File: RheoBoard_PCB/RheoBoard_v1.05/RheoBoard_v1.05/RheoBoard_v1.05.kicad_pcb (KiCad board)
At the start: 2 copper layers, 109 x 126.4 mm, 160 parts, among them J1 JST SH 4-pin 1.00mm, J12 JST SH 4-pin 1.00mm, J17 JST SH 4-pin 1.00mm, J19 BUTTONS_GPIO, J2 PJ-082BH, J3 JST EH 4-pin 2.50mm, J9 JST SH 4-pin 1.00mm, Q10 AO3400A, Q11 DMP6023LE-13, Q3 AO3400A, Q4 AO3400A, Q8 AO3400A, SW1 TL3301NF160QG/P010515, SW2 TL3301NF160QG/P010515, SW3 TL3301NF160QG/P010515, SW4 TL3301NF160QG/P010515, U1 TPS563203DRLR, U10 JST XH 2-pin 2.50mm, U11 ZR370-02PM / 4.5V / 2.5 LPM /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, U12 TPS259472ARPWR, U13 TCA9517ADGKR, U2 TPS563203DRLR, U3 TPS563203DRLR, U5 MPRLS0025PA00001A, U7 PCA9685PW,118, U8 ZR370-02PM / 4.5V / 2.5 LPM /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, U9 JST XH 2-pin 2.50mm

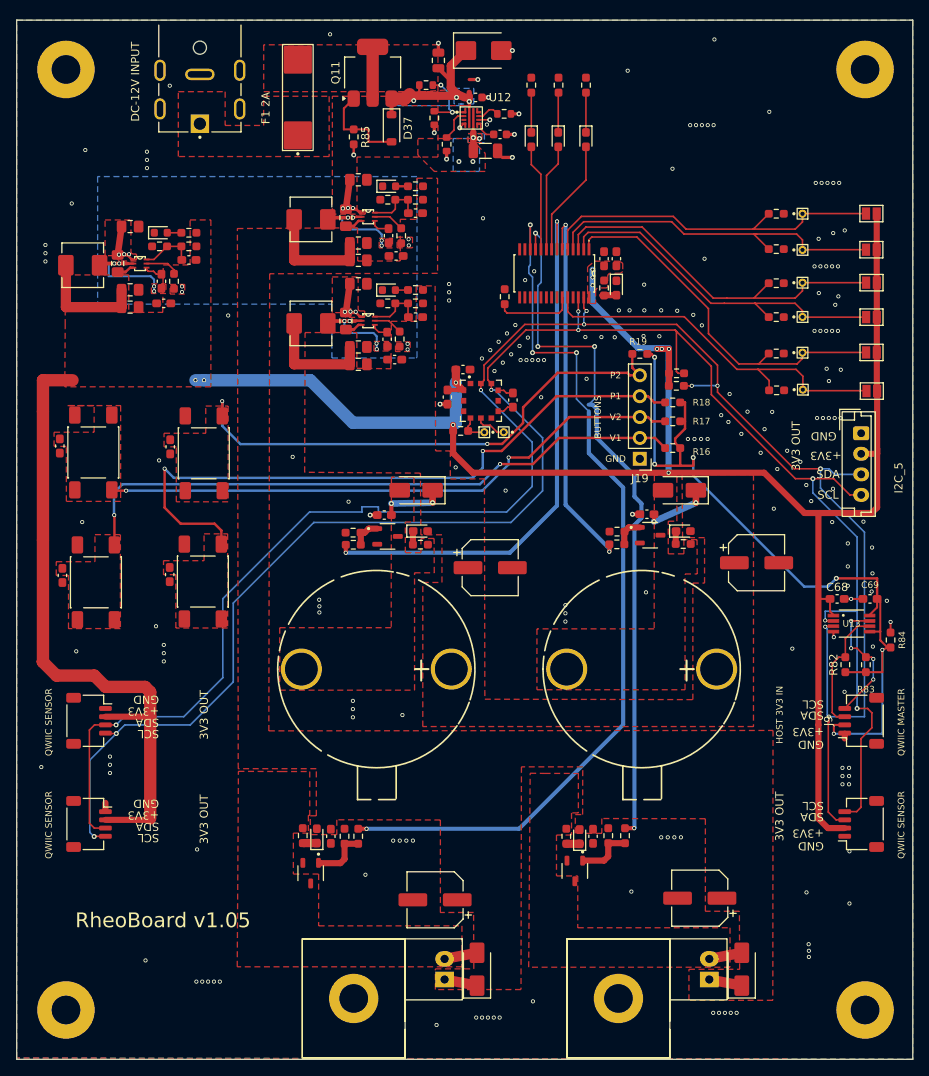
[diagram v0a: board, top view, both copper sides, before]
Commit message: Update RheoBoard v1.05 documentation and manufacturing files. Refined assembly and bringup notes to include updated LED polarity and connector specifications. Corrected footprint and layout details based on recent reviews, ensuring alignment with TI recommendations. Enhanced revision notes to reflect changes in component placements and routing adjustments, including improved via organization and updated BOM references. Manufacturing files, including Gerber and assembly drawings, have been refreshed for accuracy in production.
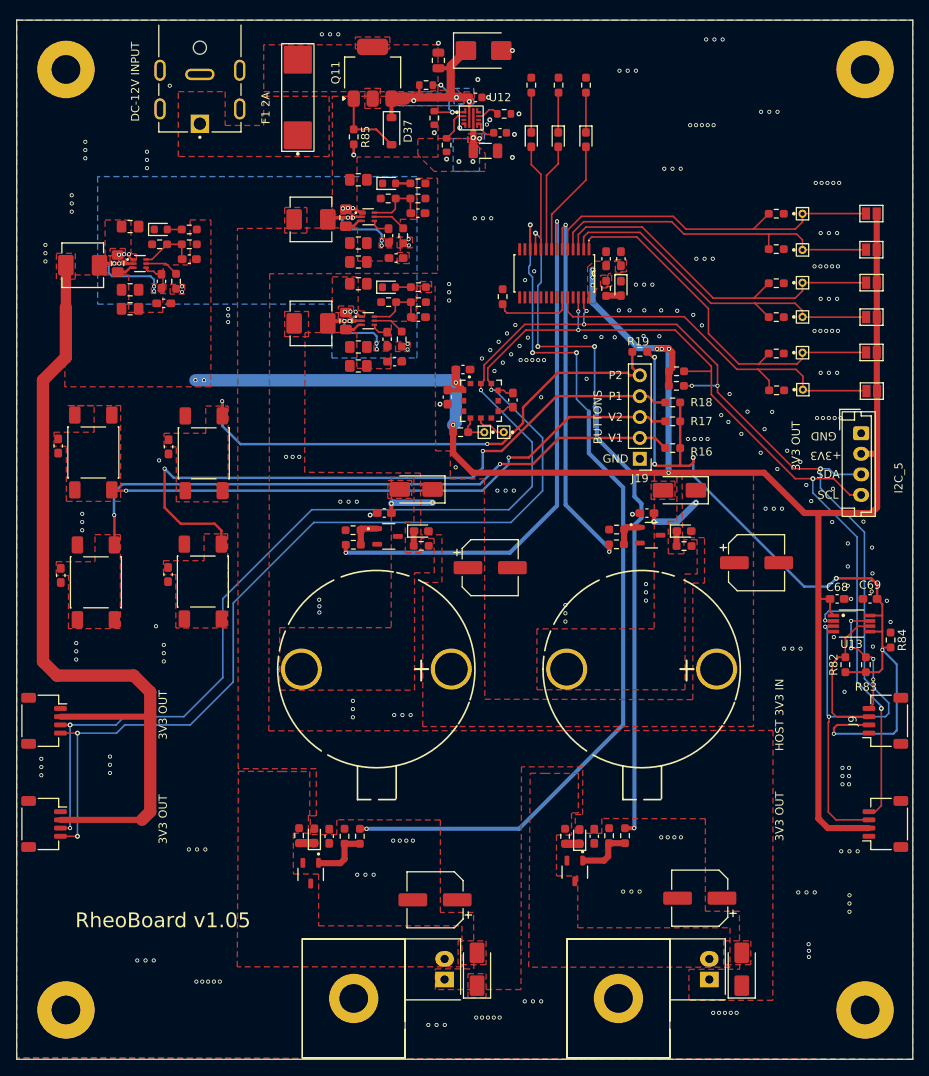
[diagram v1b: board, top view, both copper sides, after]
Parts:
- D13, D14, D15, D17, D19, D6, D7, D8: footprint LED_SMD:LED_0603_1608Metric_Pad1.05x0.95mm_HandSolder -> RheoBoard:LED_SZYY0603R_A1_K2_HandSolder
- D33, D34, D35: footprint LED_SMD:LED_0603_1608Metric -> RheoBoard:LED_SZYY0603R_A1_K2_Nominal
- moved J1 5.47 mm to (92.5, 136.4)
- moved J17 5.47 mm to (92.5, 123.8)
- moved J12 2.95 mm to (194.9, 136.4)
- moved J9 2.95 mm to (194.9, 123.8)
- moved D15 0.55 mm to (162.7, 71.2)
- moved C29 0.55 mm to (162.7, 67.6)
- moved R73 0.49 mm to (138.1, 71.1)
- moved R75 0.46 mm to (138.0, 58.5)
- moved R54 0.45 mm to (123.6, 137.8)
- moved R77 0.40 mm to (110.2, 64.1)
- moved D35 0.40 mm to (106.7, 64.1)
- moved R45 0.38 mm to (138.1, 72.9)
- moved D33 0.35 mm to (134.5, 71.1)
- moved D37 0.35 mm to (134.8, 52.1)
- moved C55 0.35 mm to (138.1, 74.7)
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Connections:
- D13 pad 1: Net-(D13-K) -> +4V5
- D13 pad 2: +4V5 -> Net-(D13-K)
- D14 pad 1: Net-(D14-K) -> +4V5
- D14 pad 2: +4V5 -> Net-(D14-K)
- D15 pad 1: GND -> Net-(D15-A)
- D15 pad 2: Net-(D15-A) -> GND
- D17 pad 1: Net-(D17-K) -> +6V
- D17 pad 2: +6V -> Net-(D17-K)
- D19 pad 1: Net-(D19-K) -> +6V
- D19 pad 2: +6V -> Net-(D19-K)
- D33 pad 1: GND -> Net-(D33-A)
- D33 pad 2: Net-(D33-A) -> GND
- D34 pad 1: GND -> Net-(D34-A)
- D34 pad 2: Net-(D34-A) -> GND
- D35 pad 1: GND -> Net-(D35-A)
- D35 pad 2: Net-(D35-A) -> GND
- D6 pad 1: Net-(D6-K) -> /PUMP2_PWM
- D6 pad 2: /PUMP2_PWM -> Net-(D6-K)
- D7 pad 1: Net-(D7-K) -> /PUMP3_PWM
- D7 pad 2: /PUMP3_PWM -> Net-(D7-K)
- D8 pad 1: Net-(D8-K) -> /PUMP4_PWM
- D8 pad 2: /PUMP4_PWM -> Net-(D8-K)
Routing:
- net +6V: track 21.9 -> 0.00 mm
- net GND: track 27.8 -> 7.76 mm, vias 203 -> 263
- net +4V5: track 29.8 -> 13.3 mm
- net VIN: track 20.5 -> 6.60 mm
- net +3V3: track 314.5 -> 323.4 mm
- net /SDA: track 233.0 -> 241.4 mm, vias 9 -> 10
- net Net-(D1-A): track 6.30 -> 0.00 mm
- net Net-(D18-A): track 4.02 -> 0.00 mm
- net Net-(D16-A): track 4.02 -> 0.00 mm
- net /HOST_SDA: track 15.3 -> 18.3 mm
- net Net-(D37-A): track 11.5 -> 9.11 mm
- net /HOST_3V3: track 99.6 -> 101.1 mm
- net /HOST_SCL: track 16.2 -> 15.0 mm
- net /A3: track 43.3 -> 42.2 mm
- net VALVE1: track 86.4 -> 85.6 mm
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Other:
- board text removed: "QWIIC MASTER"
- board text removed: "QWIIC SENSOR"

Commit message: Update RheoBoard v1.05 documentation and remove obsolete files. Enhanced README for clarity on project versions and updated assembly notes. Removed outdated files related to v0.05-altium and v1.05, including assembly and footprint documentation, to streamline project structure. Added local ignore rules for PCB diagnostics and updated BOM references for accuracy in production.
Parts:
- J3: footprint Connector_JST:JST_EH_B4B-EH-A_1x04_P2.50mm_Vertical -> RheoBoard:JST_EH_B4B-EH-A_1x04_P2.50mm_Vertical_DFM
- Q11: footprint Package_TO_SOT_SMD:SOT-223-3_TabPin2 -> RheoBoard:SOT-223-3_TabPin2_DFM
- Q3: footprint RheoBoard:AO3400A -> RheoBoard:AO3400A_Pin1Offset
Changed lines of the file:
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@@
 		(embedded_fonts no)
 	)
-	(footprint "Package_TO_SOT_SMD:SOT-223-3_TabPin2"
+	(footprint "RheoBoard:SOT-223-3_TabPin2_DFM"
 		(layer "F.Cu")
 		(at 132.5 45 90)
@@
 		)
 	)
-	(footprint "Connector_JST:JST_EH_B4B-EH-A_1x04_P2.50mm_Vertical"
+	(footprint "RheoBoard:JST_EH_B4B-EH-A_1x04_P2.50mm_Vertical_DFM"
 		(layer "F.Cu")
 		(at 191.925 88.85 -90)
@@
 		)
 	)
-	(footprint "RheoBoard:AO3400A"
+	(footprint "RheoBoard:AO3400A_Pin1Offset"
 		(layer "F.Cu")
 		(at 166.255 101.25)
@@
 		(drill 0.3)
 		(layers "F.Cu" "B.Cu")
+		(teardrops
+			(best_length_ratio 0.5)
+			(max_length 1)
+			(best_width_ratio 1)
+			(max_width 2)
+			(curved_edges no)
+			(filter_ratio 0.9)
+			(enabled yes)
+			(allow_two_segments yes)
+			(prefer_zone_connections yes)
+		)
 		(net "GND")
 	)
@@
 		(drill 0.3)
 		(layers "F.Cu" "B.Cu")
+		(teardrops
+			(best_length_ratio 0.5)
+			(max_length 1)
+			(best_width_ratio 1)
+			(max_width 2)
+			(curved_edges no)
+			(filter_ratio 0.9)
+			(enabled yes)
+			(allow_two_segments yes)
+			(prefer_zone_connections yes)
+		)
 		(net "GND")
 	)
@@
 		(drill 0.3)
 		(layers "F.Cu" "B.Cu")
+		(teardrops
+			(best_length_ratio 0.5)
+			(max_length 1)
+			(best_width_ratio 1)
+			(max_width 2)
+			(curved_edges no)
+			(filter_ratio 0.9)
+			(enabled yes)
+			(allow_two_segments yes)
+			(prefer_zone_connections yes)
+		)
 		(net "GND")
 	)
@@
 		(drill 0.3)
 		(layers "F.Cu" "B.Cu")
+		(teardrops
+			(best_length_ratio 0.5)
+			(max_length 1)
+			(best_width_ratio 1)
+			(max_width 2)
+			(curved_edges no)
+			(filter_ratio 0.9)
+			(enabled yes)
+			(allow_two_segments yes)
+			(prefer_zone_connections yes)
+		)
 		(net "GND")
 	)
@@
 		(drill 0.3)
 		(layers "F.Cu" "B.Cu")
+		(teardrops
+			(best_length_ratio 0.5)
+			(max_length 1)
+			(best_width_ratio 1)
+			(max_width 2)
+			(curved_edges no)
+			(filter_ratio 0.9)
+			(enabled yes)
+			(allow_two_segments yes)
+			(prefer_zone_connections yes)
+		)
 		(net "GND")
 	)
@@
 		(drill 0.3)
 		(layers "F.Cu" "B.Cu")
+		(teardrops
+			(best_length_ratio 0.5)
+			(max_length 1)
+			(best_width_ratio 1)
+			(max_width 2)
+			(curved_edges no)
+			(filter_ratio 0.9)
+			(enabled yes)
+			(allow_two_segments yes)
+			(prefer_zone_connections yes)
+		)
 		(net "GND")
 	)
@@
 		(drill 0.3)
 		(layers "F.Cu" "B.Cu")
+		(teardrops
+			(best_length_ratio 0.5)
+			(max_length 1)
+			(best_width_ratio 1)
+			(max_width 2)
+			(curved_edges no)
+			(filter_ratio 0.9)
+			(enabled yes)
+			(allow_two_segments yes)
+			(prefer_zone_connections yes)
+		)
 		(net "GND")
 	)
@@
 		(drill 0.3)
 		(layers "F.Cu" "B.Cu")
+		(teardrops
+			(best_length_ratio 0.5)
+			(max_length 1)
+			(best_width_ratio 1)
+			(max_width 2)
+			(curved_edges no)
+			(filter_ratio 0.9)
+			(enabled yes)
+			(allow_two_segments yes)
+			(prefer_zone_connections yes)
+		)
 		(net "GND")
 	)
@@
 		(drill 0.3)
 		(layers "F.Cu" "B.Cu")
+		(teardrops
+			(best_length_ratio 0.5)
+			(max_length 1)
+			(best_width_ratio 1)
+			(max_width 2)
+			(curved_edges no)
+			(filter_ratio 0.9)
+			(enabled yes)
+			(allow_two_segments yes)
+			(prefer_zone_connections yes)
+		)
 		(net "GND")
 	)
